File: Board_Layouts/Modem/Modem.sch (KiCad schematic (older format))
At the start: 42 parts, among them Q2 Q_PNP_CBE, T1 600:600, U1 MC1458, U2 MC1458, U3 MC1458, U4 MC1458, U5 MC1458, U6 LM555

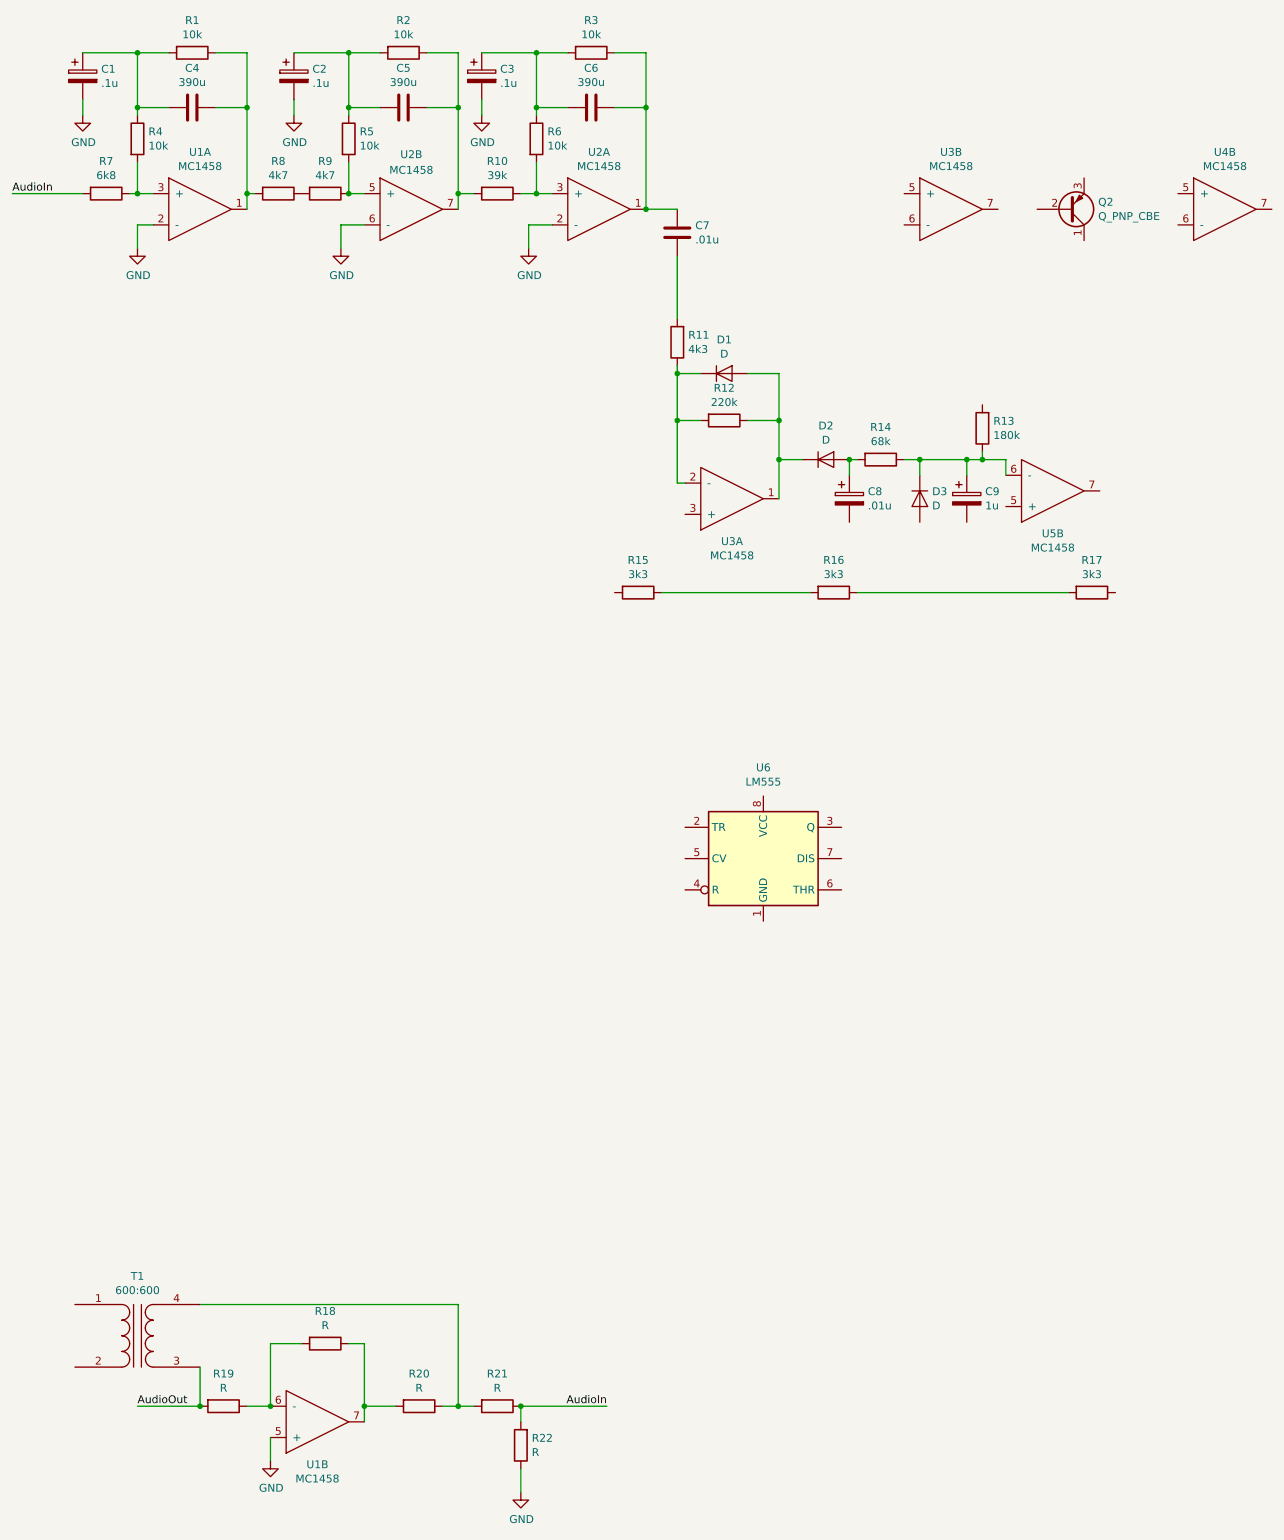
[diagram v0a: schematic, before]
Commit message: Update local changes & working on printer driver
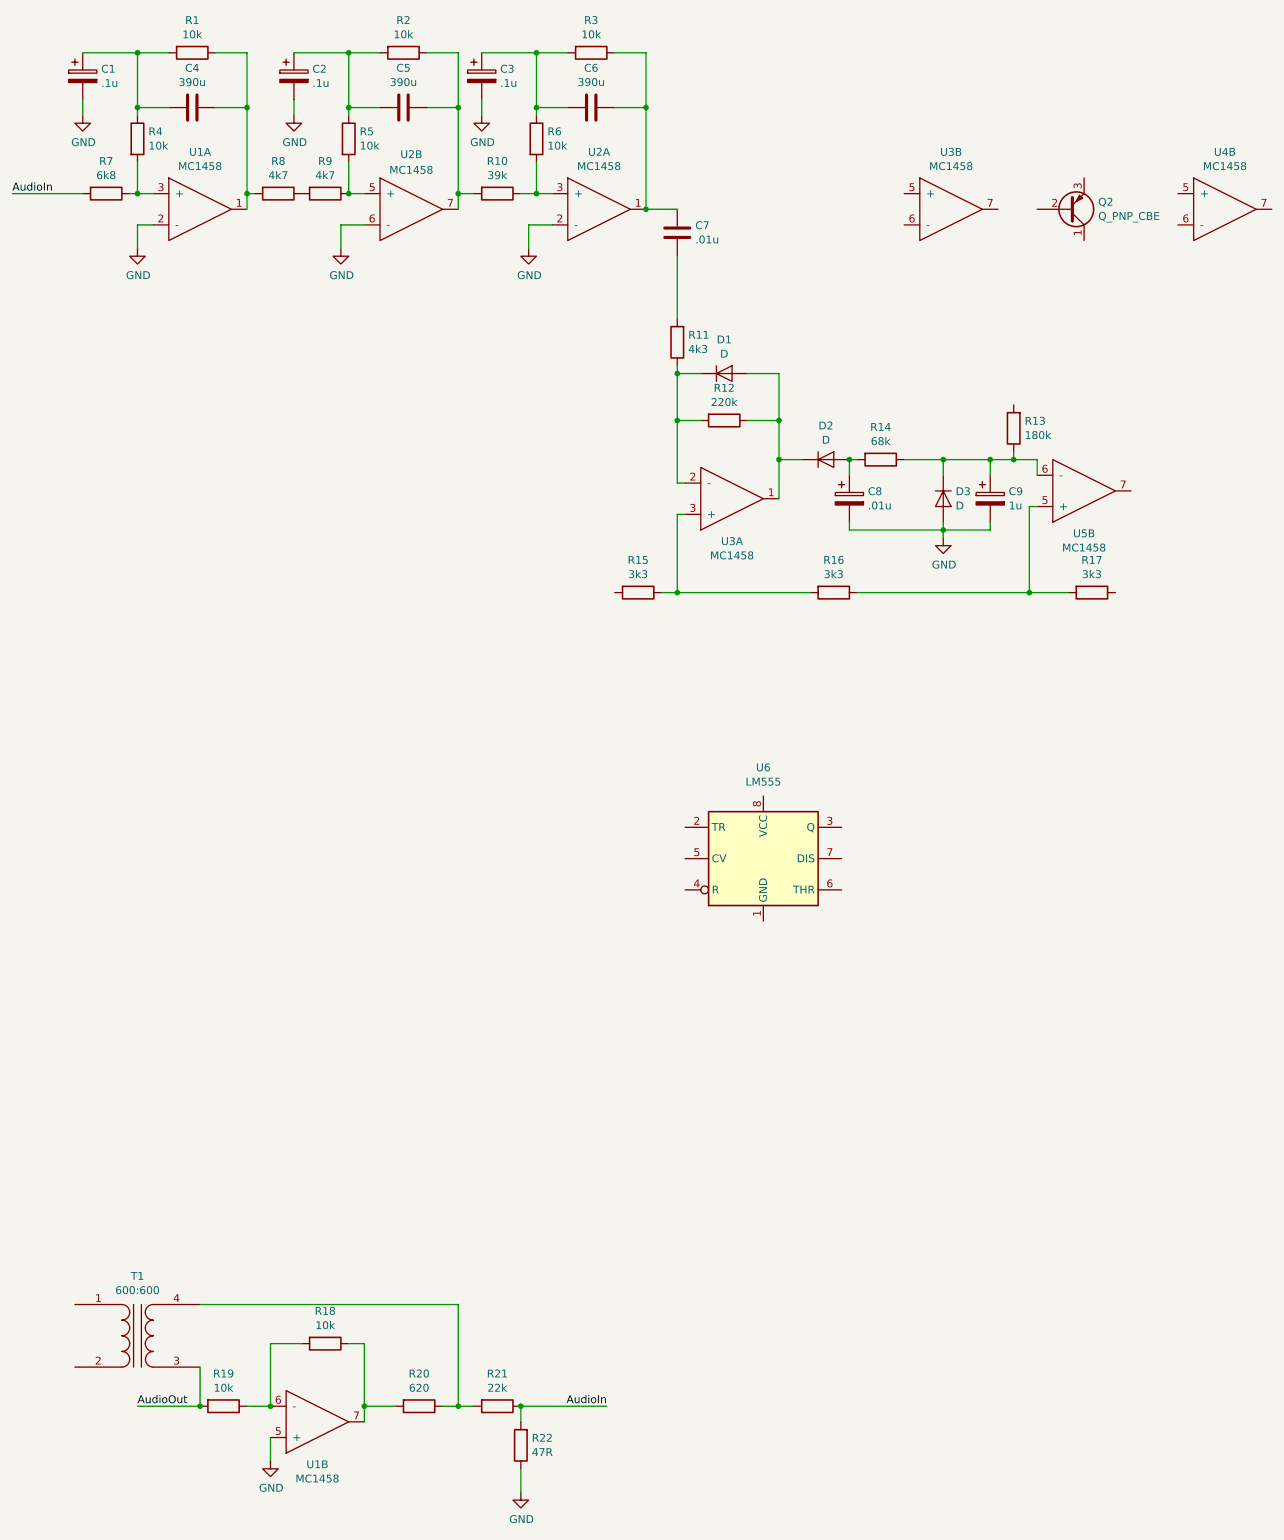
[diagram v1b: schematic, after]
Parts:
- R18, R19: value R -> 10k
- R20: value R -> 620
- R21: value R -> 22k
- R22: value R -> 47R
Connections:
- net GND: now also C8.2, C9.2, D3.2 (A)
- net at U3.3 (+): now also R15.1, R16.2
- net at U5.5 (+): now also R16.1, R17.2
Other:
- moved on the sheet: C9, D3, R13, U5B
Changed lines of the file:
@@
 L Custom_Parts:MC1458 U5
 U 2 1 5D5D3C16
-P 9300 4000
-F 0 "U5" H 9300 4273 50  0000 C CNN
-F 1 "MC1458" H 9300 4364 50  0000 C CNN
-F 2 "" H 9300 4000 50  0001 C CNN
-F 3 "" H 9300 4000 50  0001 C CNN
-	2    9300 4000
+P 9500 4000
+F 0 "U5" H 9500 4273 50  0000 C CNN
+F 1 "MC1458" H 9500 4364 50  0000 C CNN
+F 2 "" H 9500 4000 50  0001 C CNN
+F 3 "" H 9500 4000 50  0001 C CNN
+	2    9500 4000
 	1    0    0    1
 $EndComp
@@
 L Device:D D3
 U 1 1 5D5D54DA
-P 8450 4050
-F 0 "D3" V 8404 4129 50  0000 L CNN
-F 1 "D" V 8495 4129 50  0000 L CNN
-F 2 "" H 8450 4050 50  0001 C CNN
-F 3 "~" H 8450 4050 50  0001 C CNN
-	1    8450 4050
+P 8600 4050
+F 0 "D3" V 8554 4129 50  0000 L CNN
+F 1 "D" V 8645 4129 50  0000 L CNN
+F 2 "" H 8600 4050 50  0001 C CNN
+F 3 "~" H 8600 4050 50  0001 C CNN
+	1    8600 4050
 	0    1    1    0
 $EndComp
@@
 L Device:R R13
 U 1 1 5D5D9192
-P 8850 3600
-F 0 "R13" H 8780 3554 50  0000 R CNN
-F 1 "180k" H 8780 3645 50  0000 R CNN
-F 2 "" V 8780 3600 50  0001 C CNN
-F 3 "~" H 8850 3600 50  0001 C CNN
-	1    8850 3600
+P 9050 3600
+F 0 "R13" H 8980 3554 50  0000 R CNN
+F 1 "180k" H 8980 3645 50  0000 R CNN
+F 2 "" V 8980 3600 50  0001 C CNN
+F 3 "~" H 9050 3600 50  0001 C CNN
+	1    9050 3600
 	-1   0    0    1
 $EndComp
@@
 L Device:CP C9
 U 1 1 5D5DBF7C
-P 8750 4050
-F 0 "C9" H 8868 4096 50  0000 L CNN
-F 1 "1u" H 8868 4005 50  0000 L CNN
-F 2 "" H 8788 3900 50  0001 C CNN
-F 3 "~" H 8750 4050 50  0001 C CNN
-	1    8750 4050
-	1    0    0    -1
-$EndComp
-Wire Wire Line
-	6800 4650 7750 4650
-Wire Wire Line
-	8050 4650 9400 4650
+P 8900 4050
+F 0 "C9" H 9018 4096 50  0000 L CNN
+F 1 "1u" H 9018 4005 50  0000 L CNN
+F 2 "" H 8938 3900 50  0001 C CNN
+F 3 "~" H 8900 4050 50  0001 C CNN
+	1    8900 4050
+	1    0    0    -1
+$EndComp
+Wire Wire Line
+	6800 4650 6900 4650
+Wire Wire Line
+	8050 4650 9150 4650
 Wire Wire Line
 	7050 3250 6900 3250
@@
 Connection ~ 8000 3800
 Wire Wire Line
-	8350 3800 8450 3800
-Wire Wire Line
-	9000 3800 9000 3900
-Wire Wire Line
-	8850 3750 8850 3800
-Connection ~ 8850 3800
-Wire Wire Line
-	8850 3800 9000 3800
-Wire Wire Line
-	8750 3900 8750 3800
-Connection ~ 8750 3800
-Wire Wire Line
-	8750 3800 8850 3800
-Wire Wire Line
-	8450 3900 8450 3800
-Connection ~ 8450 3800
-Wire Wire Line
-	8450 3800 8750 3800
+	9200 3800 9200 3900
+Wire Wire Line
+	9050 3750 9050 3800
+Connection ~ 9050 3800
+Wire Wire Line
+	9050 3800 9200 3800
+Wire Wire Line
+	8900 3900 8900 3800
+Wire Wire Line
+	8600 3900 8600 3800
 Wire Wire Line
 	6900 2900 6900 2500
@@
 P 4000 9850
 F 0 "R19" V 3793 9850 50  0000 C CNN
-F 1 "R" V 3884 9850 50  0000 C CNN
+F 1 "10k" V 3884 9850 50  0000 C CNN
 F 2 "" V 3930 9850 50  0001 C CNN
 F 3 "~" H 4000 9850 50  0001 C CNN
@@
 P 4650 9450
 F 0 "R18" V 4443 9450 50  0000 C CNN
-F 1 "R" V 4534 9450 50  0000 C CNN
+F 1 "10k" V 4534 9450 50  0000 C CNN
 F 2 "" V 4580 9450 50  0001 C CNN
 F 3 "~" H 4650 9450 50  0001 C CNN
@@
 P 5250 9850
 F 0 "R20" V 5043 9850 50  0000 C CNN
-F 1 "R" V 5134 9850 50  0000 C CNN
+F 1 "620" V 5134 9850 50  0000 C CNN
 F 2 "" V 5180 9850 50  0001 C CNN
 F 3 "~" H 5250 9850 50  0001 C CNN
@@
 P 5750 9850
 F 0 "R21" V 5543 9850 50  0000 C CNN
-F 1 "R" V 5634 9850 50  0000 C CNN
+F 1 "22k" V 5634 9850 50  0000 C CNN
 F 2 "" V 5680 9850 50  0001 C CNN
 F 3 "~" H 5750 9850 50  0001 C CNN
@@
 P 5900 10100
 F 0 "R22" H 5830 10054 50  0000 R CNN
-F 1 "R" H 5830 10145 50  0000 R CNN
+F 1 "47R" H 5830 10145 50  0000 R CNN
 F 2 "" V 5830 10100 50  0001 C CNN
 F 3 "~" H 5900 10100 50  0001 C CNN
@@
 	3450 9850 3850 9850
 Connection ~ 3850 9850
+Wire Wire Line
+	8350 3800 8600 3800
+Wire Wire Line
+	6950 4150 6900 4150
+Wire Wire Line
+	6900 4150 6900 4650
+Connection ~ 6900 4650
+Wire Wire Line
+	6900 4650 7750 4650
+Wire Wire Line
+	9200 4100 9150 4100
+Wire Wire Line
+	9150 4100 9150 4650
+Connection ~ 9150 4650
+Wire Wire Line
+	9150 4650 9400 4650
+Connection ~ 8600 3800
+Wire Wire Line
+	8600 3800 8900 3800
+Connection ~ 8900 3800
+Wire Wire Line
+	8900 3800 9050 3800
+Wire Wire Line
+	8000 4200 8000 4250
+Wire Wire Line
+	8900 4250 8900 4200
+Wire Wire Line
+	8600 4200 8600 4250
+$Comp
+L power:GND #PWR?
+U 1 1 5D7D11E1
+P 8600 4300
+F 0 "#PWR?" H 8600 4050 50  0001 C CNN
+F 1 "GND" H 8605 4127 50  0000 C CNN
+F 2 "" H 8600 4300 50  0001 C CNN
+F 3 "" H 8600 4300 50  0001 C CNN
+	1    8600 4300
+	1    0    0    -1
+$EndComp
+Wire Wire Line
+	8000 4250 8600 4250
+Connection ~ 8600 4250
+Wire Wire Line
+	8600 4250 8600 4300
+Wire Wire Line
+	8600 4250 8900 4250
 $EndSCHEMATC
